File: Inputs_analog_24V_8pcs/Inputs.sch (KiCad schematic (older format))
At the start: 88 parts, among them J10 Screw_Terminal_01x03, J11 Screw_Terminal_01x03, J4 Screw_Terminal_01x03, J5 Screw_Terminal_01x03, J6 Screw_Terminal_01x03, J7 Screw_Terminal_01x03, J8 Screw_Terminal_01x03, J9 Screw_Terminal_01x03, U10 4N28, U11 4N28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

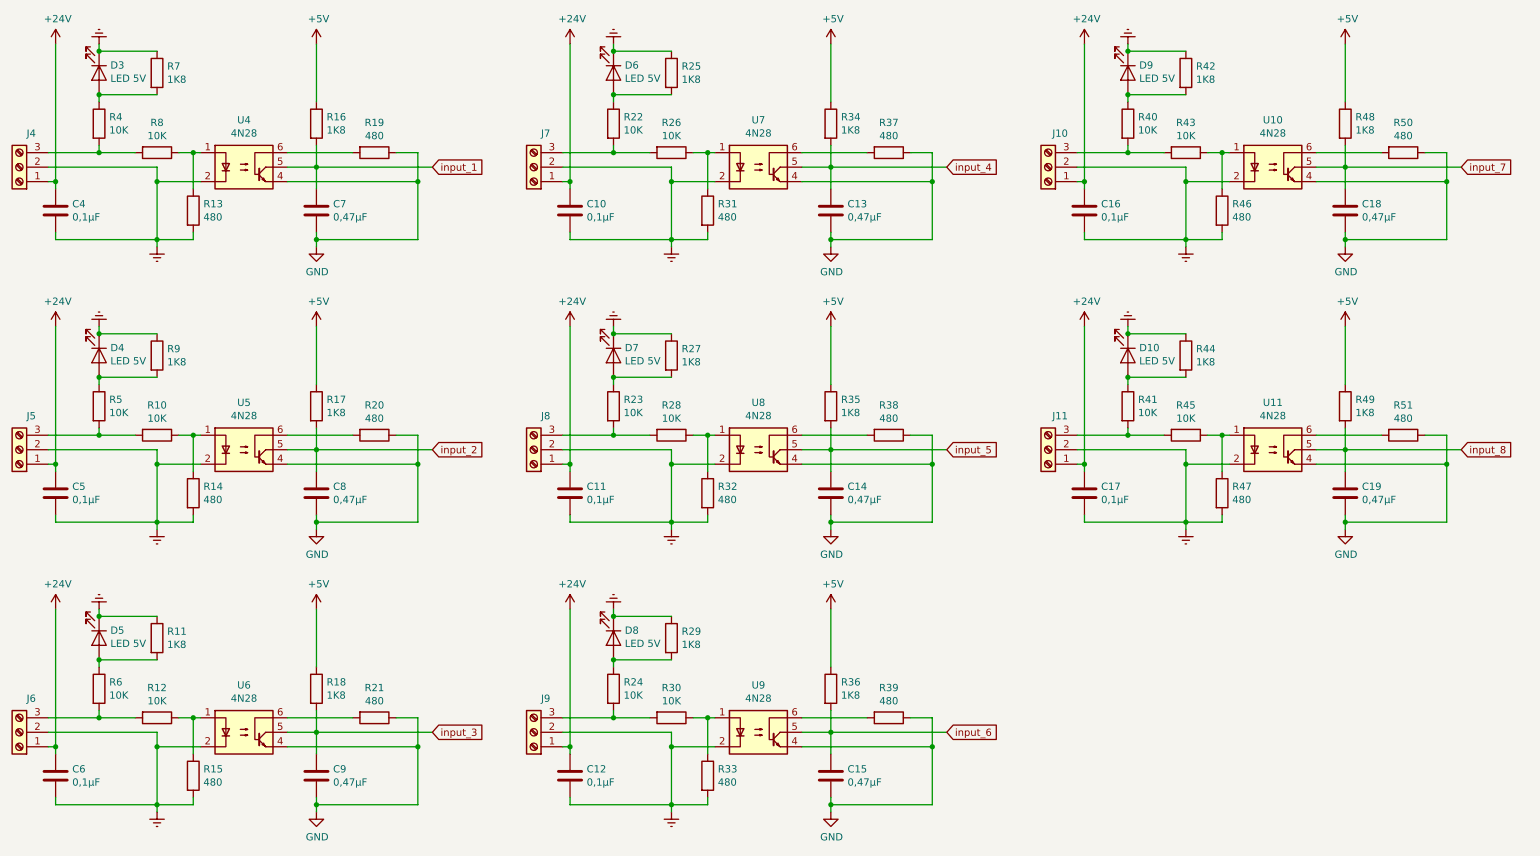
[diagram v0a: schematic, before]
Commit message: Update scmematics Add pcb second layer
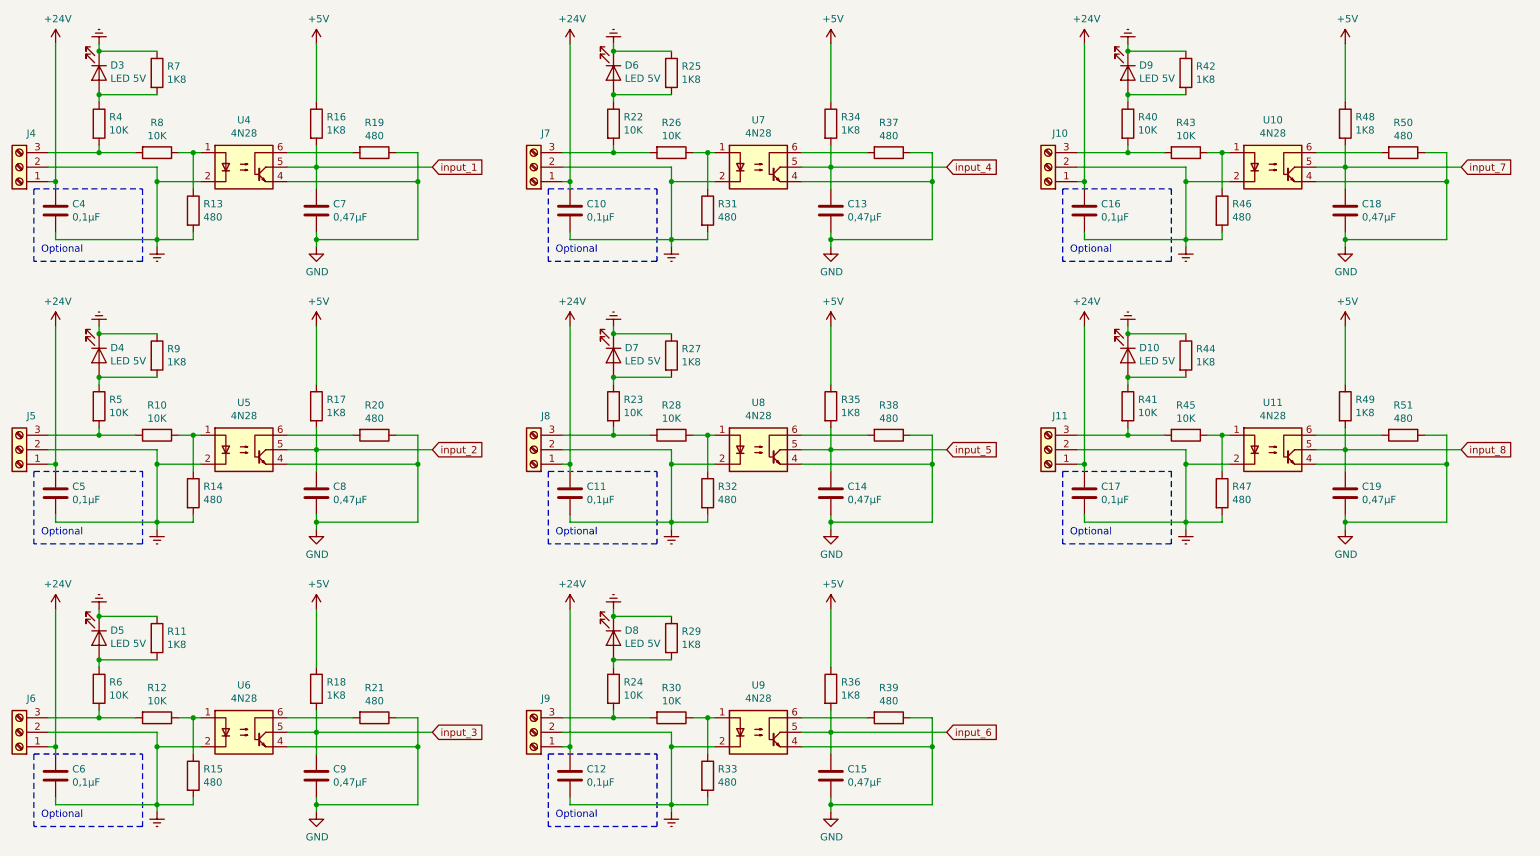
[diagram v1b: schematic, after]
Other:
- note added: "Optional"

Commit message: Update Inputs pcb
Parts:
- D10, D3, D4, D5, D6, D7, D8, D9: footprint Diode_THT:D_A-405_P2.54mm_Vertical_AnodeUp -> LED_THT:LED_D3.0mm
- J10, J11, J4, J5, J6, J7, J8, J9: footprint Connector_PinHeader_2.54mm:PinHeader_1x03_P2.54mm_Horizontal -> Connector_PinHeader_2.54mm:PinHeader_1x03_P2.54mm_Vertical
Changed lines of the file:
@@
 EESchema Schematic File Version 4
-EELAYER 30 0
+LIBS:Inputs_analog_24V_8pcs-cache
+EELAYER 26 0
 EELAYER END
 $Descr A4 11693 8268
@@
 F 0 "D3" V 1247 1128 50  0000 L CNN
 F 1 "LED 5V" V 1338 1128 50  0000 L CNN
-F 2 "Diode_THT:D_A-405_P2.54mm_Vertical_AnodeUp" H 1300 1050 50  0001 C CNN
+F 2 "LED_THT:LED_D3.0mm" H 1300 1050 50  0001 C CNN
 F 3 "~" H 1300 1050 50  0001 C CNN
 	1    1300 1050
@@
 F 0 "J5" H 668 3417 50  0000 C CNN
 F 1 "Screw_Terminal_01x03" H 668 3416 50  0001 C CNN
-F 2 "Connector_PinHeader_2.54mm:PinHeader_1x03_P2.54mm_Horizontal" H 750 3650 50  0001 C CNN
+F 2 "Connector_PinHeader_2.54mm:PinHeader_1x03_P2.54mm_Vertical" H 750 3650 50  0001 C CNN
 F 3 "~" H 750 3650 50  0001 C CNN
 	1    750  3650
@@
 F 0 "D4" V 1247 3078 50  0000 L CNN
 F 1 "LED 5V" V 1338 3078 50  0000 L CNN
-F 2 "Diode_THT:D_A-405_P2.54mm_Vertical_AnodeUp" H 1300 3000 50  0001 C CNN
+F 2 "LED_THT:LED_D3.0mm" H 1300 3000 50  0001 C CNN
 F 3 "~" H 1300 3000 50  0001 C CNN
 	1    1300 3000
@@
 F 0 "J6" H 668 5367 50  0000 C CNN
 F 1 "Screw_Terminal_01x03" H 668 5366 50  0001 C CNN
-F 2 "Connector_PinHeader_2.54mm:PinHeader_1x03_P2.54mm_Horizontal" H 750 5600 50  0001 C CNN
+F 2 "Connector_PinHeader_2.54mm:PinHeader_1x03_P2.54mm_Vertical" H 750 5600 50  0001 C CNN
 F 3 "~" H 750 5600 50  0001 C CNN
 	1    750  5600
@@
 F 0 "D5" V 1247 5028 50  0000 L CNN
 F 1 "LED 5V" V 1338 5028 50  0000 L CNN
-F 2 "Diode_THT:D_A-405_P2.54mm_Vertical_AnodeUp" H 1300 4950 50  0001 C CNN
+F 2 "LED_THT:LED_D3.0mm" H 1300 4950 50  0001 C CNN
 F 3 "~" H 1300 4950 50  0001 C CNN
 	1    1300 4950
@@
 F 0 "J8" H 4218 3417 50  0000 C CNN
 F 1 "Screw_Terminal_01x03" H 4218 3416 50  0001 C CNN
-F 2 "Connector_PinHeader_2.54mm:PinHeader_1x03_P2.54mm_Horizontal" H 4300 3650 50  0001 C CNN
+F 2 "Connector_PinHeader_2.54mm:PinHeader_1x03_P2.54mm_Vertical" H 4300 3650 50  0001 C CNN
 F 3 "~" H 4300 3650 50  0001 C CNN
 	1    4300 3650
@@
 F 0 "D7" V 4797 3078 50  0000 L CNN
 F 1 "LED 5V" V 4888 3078 50  0000 L CNN
-F 2 "Diode_THT:D_A-405_P2.54mm_Vertical_AnodeUp" H 4850 3000 50  0001 C CNN
+F 2 "LED_THT:LED_D3.0mm" H 4850 3000 50  0001 C CNN
 F 3 "~" H 4850 3000 50  0001 C CNN
 	1    4850 3000
@@
 F 0 "J9" H 4218 5367 50  0000 C CNN
 F 1 "Screw_Terminal_01x03" H 4218 5366 50  0001 C CNN
-F 2 "Connector_PinHeader_2.54mm:PinHeader_1x03_P2.54mm_Horizontal" H 4300 5600 50  0001 C CNN
+F 2 "Connector_PinHeader_2.54mm:PinHeader_1x03_P2.54mm_Vertical" H 4300 5600 50  0001 C CNN
 F 3 "~" H 4300 5600 50  0001 C CNN
 	1    4300 5600
@@
 F 0 "D8" V 4797 5028 50  0000 L CNN
 F 1 "LED 5V" V 4888 5028 50  0000 L CNN
-F 2 "Diode_THT:D_A-405_P2.54mm_Vertical_AnodeUp" H 4850 4950 50  0001 C CNN
+F 2 "LED_THT:LED_D3.0mm" H 4850 4950 50  0001 C CNN
 F 3 "~" H 4850 4950 50  0001 C CNN
 	1    4850 4950
@@
 F 0 "J10" H 7768 1467 50  0000 C CNN
 F 1 "Screw_Terminal_01x03" H 7768 1466 50  0001 C CNN
-F 2 "Connector_PinHeader_2.54mm:PinHeader_1x03_P2.54mm_Horizontal" H 7850 1700 50  0001 C CNN
+F 2 "Connector_PinHeader_2.54mm:PinHeader_1x03_P2.54mm_Vertical" H 7850 1700 50  0001 C CNN
 F 3 "~" H 7850 1700 50  0001 C CNN
 	1    7850 1700
@@
 F 0 "D9" V 8347 1128 50  0000 L CNN
 F 1 "LED 5V" V 8438 1128 50  0000 L CNN
-F 2 "Diode_THT:D_A-405_P2.54mm_Vertical_AnodeUp" H 8400 1050 50  0001 C CNN
+F 2 "LED_THT:LED_D3.0mm" H 8400 1050 50  0001 C CNN
 F 3 "~" H 8400 1050 50  0001 C CNN
 	1    8400 1050
@@
 F 0 "J11" H 7768 3417 50  0000 C CNN
 F 1 "Screw_Terminal_01x03" H 7768 3416 50  0001 C CNN
-F 2 "Connector_PinHeader_2.54mm:PinHeader_1x03_P2.54mm_Horizontal" H 7850 3650 50  0001 C CNN
+F 2 "Connector_PinHeader_2.54mm:PinHeader_1x03_P2.54mm_Vertical" H 7850 3650 50  0001 C CNN
 F 3 "~" H 7850 3650 50  0001 C CNN
 	1    7850 3650
@@
 F 0 "D10" V 8347 3078 50  0000 L CNN
 F 1 "LED 5V" V 8438 3078 50  0000 L CNN
-F 2 "Diode_THT:D_A-405_P2.54mm_Vertical_AnodeUp" H 8400 3000 50  0001 C CNN
+F 2 "LED_THT:LED_D3.0mm" H 8400 3000 50  0001 C CNN
 F 3 "~" H 8400 3000 50  0001 C CNN
 	1    8400 3000
@@
 F 0 "D6" V 4797 1128 50  0000 L CNN
 F 1 "LED 5V" V 4888 1128 50  0000 L CNN
-F 2 "Diode_THT:D_A-405_P2.54mm_Vertical_AnodeUp" H 4850 1050 50  0001 C CNN
+F 2 "LED_THT:LED_D3.0mm" H 4850 1050 50  0001 C CNN
 F 3 "~" H 4850 1050 50  0001 C CNN
 	1    4850 1050
@@
 F 0 "J7" H 4218 1467 50  0000 C CNN
 F 1 "Screw_Terminal_01x03" H 4218 1466 50  0001 C CNN
-F 2 "Connector_PinHeader_2.54mm:PinHeader_1x03_P2.54mm_Horizontal" H 4300 1700 50  0001 C CNN
+F 2 "Connector_PinHeader_2.54mm:PinHeader_1x03_P2.54mm_Vertical" H 4300 1700 50  0001 C CNN
 F 3 "~" H 4300 1700 50  0001 C CNN
 	1    4300 1700
@@
 F 0 "J4" H 668 1467 50  0000 C CNN
 F 1 "Screw_Terminal_01x03" H 668 1466 50  0001 C CNN
-F 2 "Connector_PinHeader_2.54mm:PinHeader_1x03_P2.54mm_Horizontal" H 750 1700 50  0001 C CNN
+F 2 "Connector_PinHeader_2.54mm:PinHeader_1x03_P2.54mm_Vertical" H 750 1700 50  0001 C CNN
 F 3 "~" H 750 1700 50  0001 C CNN
 	1    750  1700

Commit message: Change footprints for ternimals
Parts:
- J4: footprint Connector_PinHeader_2.54mm:PinHeader_1x03_P2.54mm_Vertical -> TerminalBlock_MetzConnect:TerminalBlock_MetzConnect_Type011_RT05503HBWC_1x03_P5.00mm_Horizontal
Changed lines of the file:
@@
 EESchema Schematic File Version 4
-LIBS:Inputs_analog_24V_8pcs-cache
-EELAYER 26 0
+EELAYER 30 0
 EELAYER END
 $Descr A4 11693 8268
@@
 F 0 "J4" H 668 1467 50  0000 C CNN
 F 1 "Screw_Terminal_01x03" H 668 1466 50  0001 C CNN
-F 2 "Connector_PinHeader_2.54mm:PinHeader_1x03_P2.54mm_Vertical" H 750 1700 50  0001 C CNN
+F 2 "TerminalBlock_MetzConnect:TerminalBlock_MetzConnect_Type011_RT05503HBWC_1x03_P5.00mm_Horizontal" H 750 1700 50  0001 C CNN
 F 3 "~" H 750 1700 50  0001 C CNN
 	1    750  1700
